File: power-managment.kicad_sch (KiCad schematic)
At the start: 10 parts, among them J4 ARM, J5 BATTERY, U4 MPM3610GQV-P

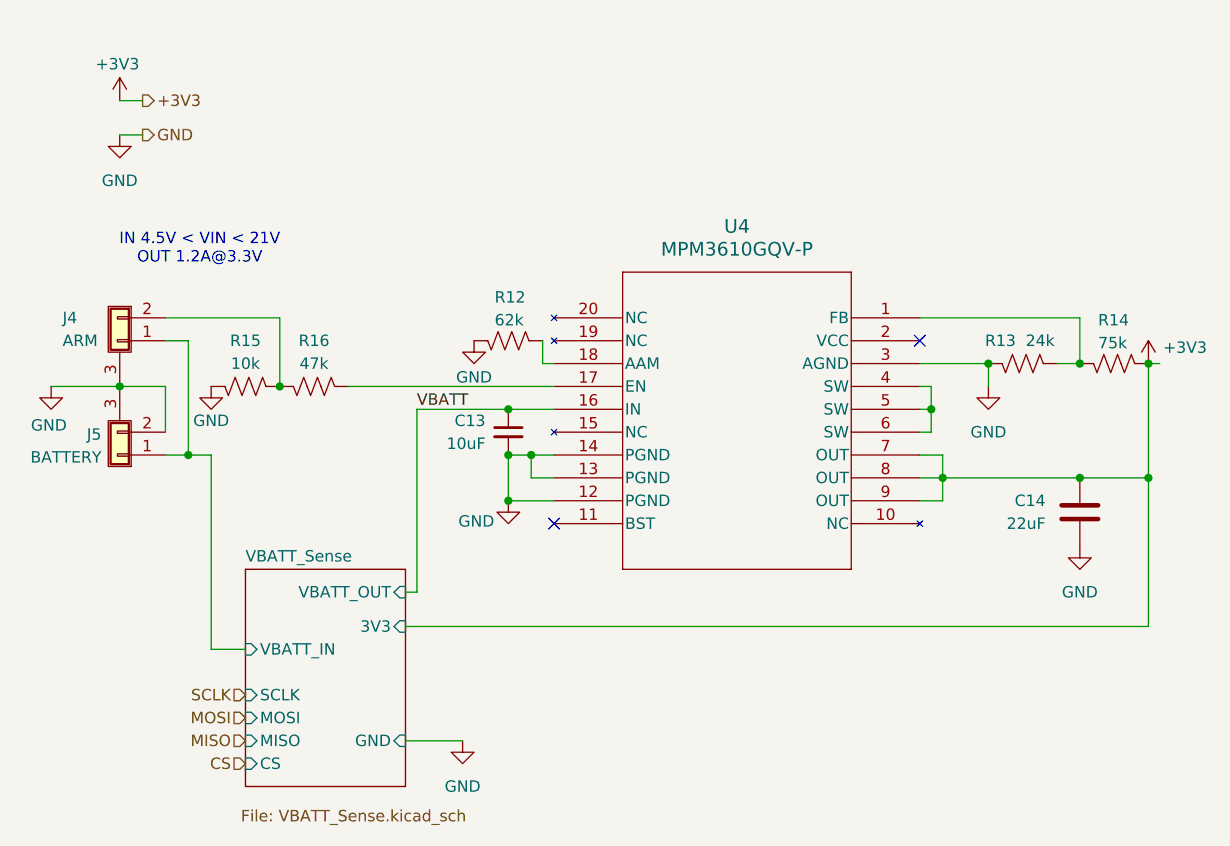
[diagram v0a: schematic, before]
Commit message: Connected topsheet
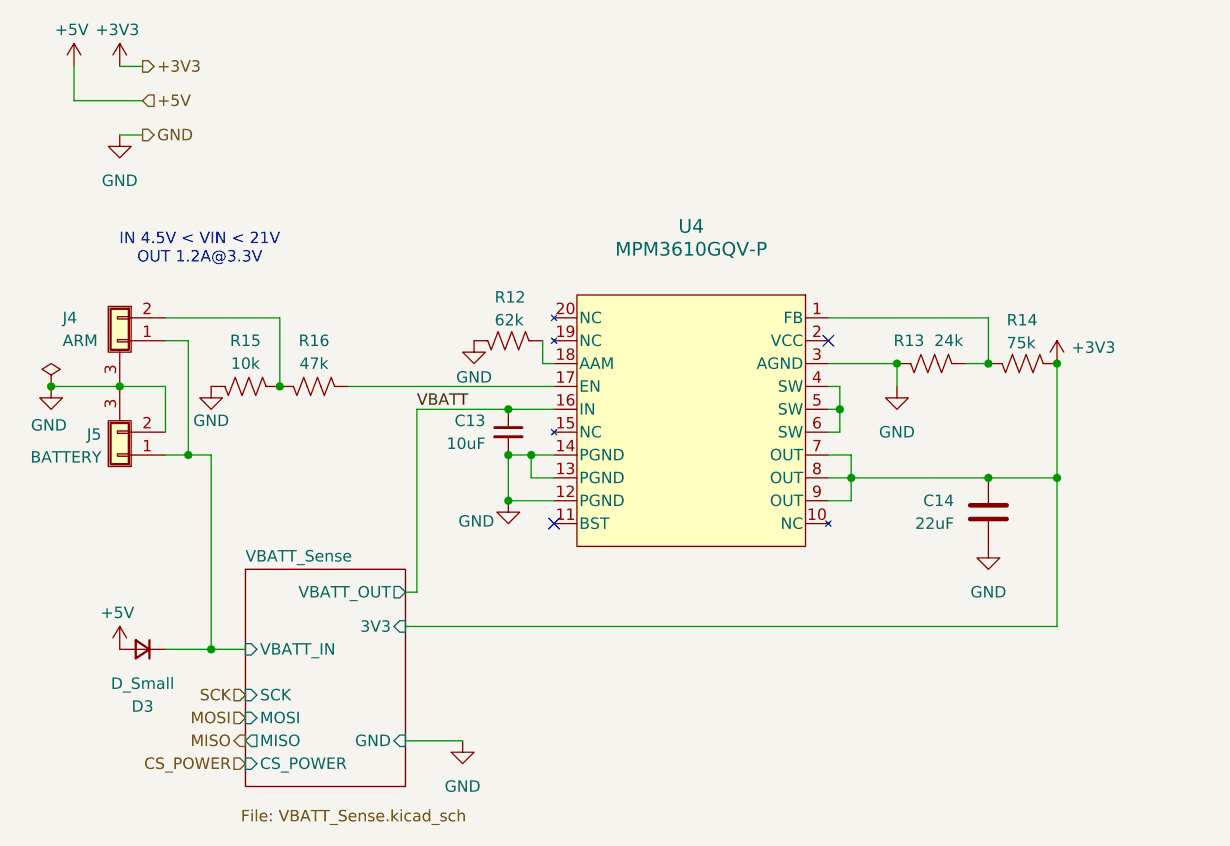
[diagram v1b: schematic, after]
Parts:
- added D3: D_Small, symbol Device:D_Small
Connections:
- net VBATT_Sense/VBATT_IN: now also D3.1 (K)
- new net +5V: D3.2 (A)
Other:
- sheet VBATT_Sense ports: added CS_POWER, SCK; removed CS, SCLK
- moved on the sheet: C14, R13, R14
